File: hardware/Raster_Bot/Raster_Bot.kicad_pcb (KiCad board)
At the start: 4 copper layers, 65 x 28 mm, 66 parts, among them J1 JST_PH, J2 USB_C_Receptacle_USB2.0_16P, J3 Conn_EYESPI, J4 Conn_Motor_N20_Encoder, J6 Conn_Motor_N20_Encoder, Q1 AO3401A, Q2 AO3401A, Q3 2N7002, SW1 SW_SPDT_SH, SW2 SW_RESET, SW3 SW_BOOT, U1 AP2114H-3.3, U2 BQ24072RGT, U3 ESP32-S3-MINI-1, U4 TPS61023DRLR, U5 DRV8833PWPR

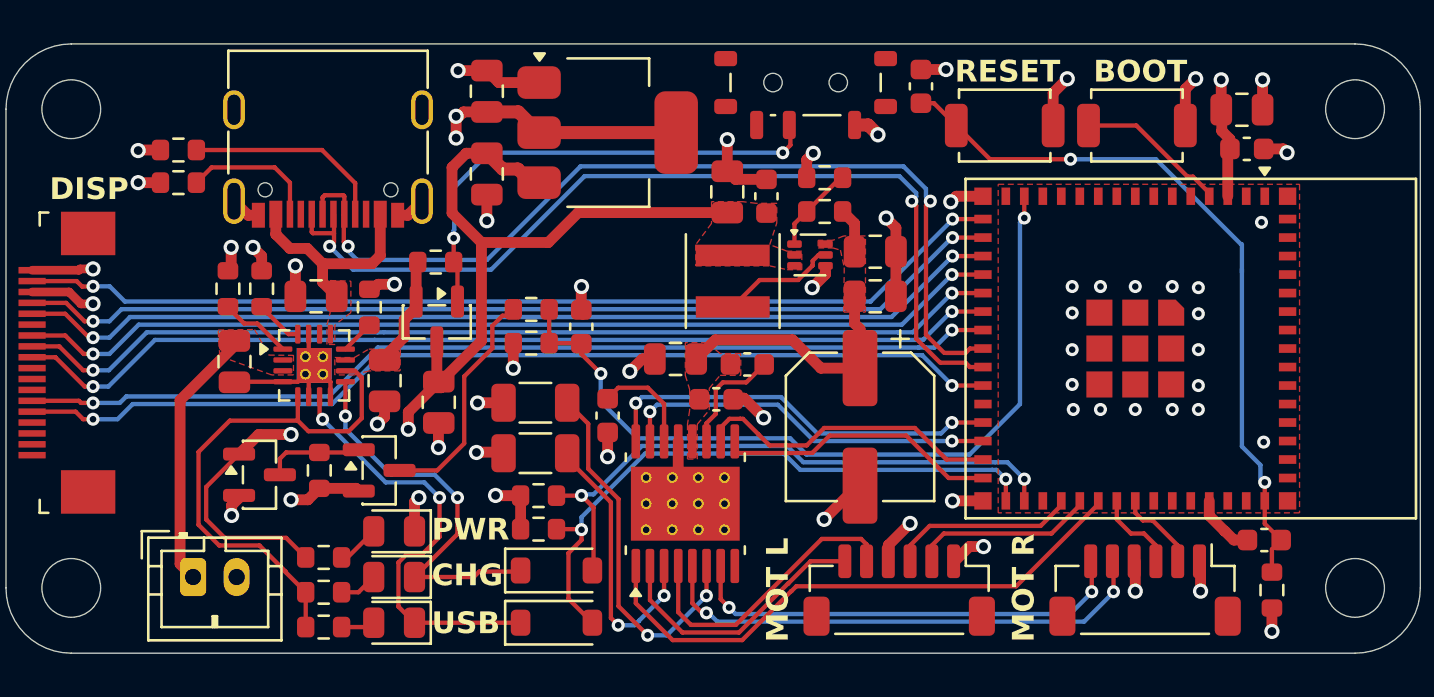
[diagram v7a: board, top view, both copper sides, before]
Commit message: [hardware] v0.7 - Added bulk capacitance; PCB layout update
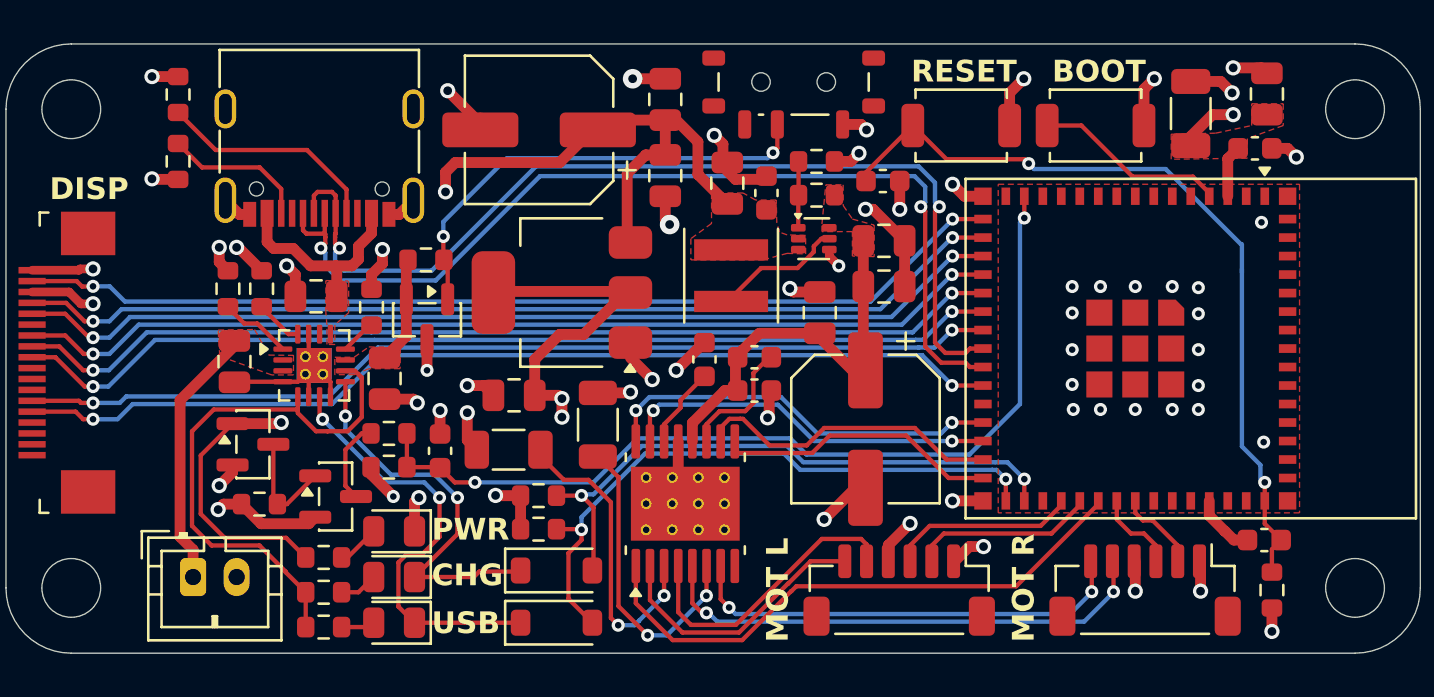
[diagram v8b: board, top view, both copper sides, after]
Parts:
- added C5: 100uF, Capacitor_SMD:C_1206_3216Metric, F.Cu at (124.5, 46.6)
- added C8: 470uF, Capacitor_SMD:CP_Elec_6.3x7.7, F.Cu at (94.5, 47.4)
- moved C12 17.4 mm to (100.3, 46.0), turned to 90 degrees
- moved C18 14.0 mm to (93.3, 59.5), turned to 180 degrees
- moved R4 8.68 mm to (87.6, 62.9)
- moved R3 8.68 mm to (87.6, 61.3)
- moved C2 8.64 mm to (90.0, 62.1)
- moved C16 8.20 mm to (100.3, 49.5)
- moved U4 7.64 mm to (95.5, 54.8), turned to 180 degrees
- moved C15 6.96 mm to (107.4, 55.8), turned to 90 degrees
- moved C11 5.14 mm to (102.1, 57.9), turned to 90 degrees
- moved C7 4.69 mm to (110.3, 49.7), turned to 0 degrees
- moved R2 3.16 mm to (81.7, 64.5), turned to 0 degrees
- moved R14 3.04 mm to (97.2, 60.9), turned to 90 degrees
- moved R6 2.55 mm to (77.9, 45.7), turned to 90 degrees
- moved Q1 2.33 mm to (85.2, 64.2)
- moved SW1 2.00 mm to (113.9, 47.1)
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- renumbered C7 to C1, C5 to C10, C16 to C11, C6 to C12, C17 to C13, C18 to C14, C19 to C15, C1 to C16, C20 to C17, C3 to C18, C8 to C19, C9 to C2, C11 to C20, C14 to C21, C15 to C22, C10 to C3, C12 to C4, C2 to C6, C13 to C7, C4 to C9, D4 to D1, D5 to D2, D1 to D3, D2 to D4, D3 to D5, J6 to J5, Q2 to Q1, Q3 to Q2, Q1 to Q3, R12 to R1, R5 to R10, R8 to R12, R18 to R13, R19 to R14, R3 to R15, R6 to R18, R7 to R19, R13 to R2, R14 to R3, R15 to R4, R1 to R5, R2 to R6, R9 to R7, R10 to R8, R4 to R9, SW2 to SW1, SW3 to SW2, SW1 to SW3, U3 to U1, U5 to U3, U1 to U4, U4 to U5
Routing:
- net GND: track 74.2 -> 84.8 mm, vias 53 -> 56
- net Net-(Q1-D): track 10.6 -> 3.84 mm
- net VSYS: track 50.5 -> 56.0 mm, vias 2 -> 3
- net /VBAT_MON: track 36.6 -> 41.8 mm
- net +5V: track 13.9 -> 18.1 mm
- net +3V3: track 27.6 -> 31.1 mm
- net /RESET: track 33.5 -> 36.8 mm
- net Net-(U3-BISEN): track 17.2 -> 14.1 mm
- net /USB_D-: track 43.2 -> 45.2 mm
- net /BOOT: track 6.98 -> 8.88 mm
- net /USB_D+: track 43.4 -> 45.0 mm
- net Net-(U3-VINT): track 5.31 -> 3.76 mm
- net VSYS_SRC: track 28.5 -> 29.7 mm
- net Net-(J2-CC1): track 9.36 -> 10.3 mm
- net Net-(U5-FB): track 4.02 -> 3.13 mm
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- added copper zone on F.Cu, net +3V3
